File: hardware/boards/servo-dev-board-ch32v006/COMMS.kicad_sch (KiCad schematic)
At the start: 9 parts, among them J7 PIN-V, J8 PIN-V, J9 JST-PH-V, U4 74LVC2G241

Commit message: fix 74LVC2G241 footprint. Pin clearance was 0.15mm. PCBWay minimum is 0.2mm. Corrent Pin width is 0.3mm with pitch of 0.5mm, leaving 0.2mm clearance. Standard KiCad Library's pin width was 0.35mm, leaving only 0.15mm of clearance, which PCBWay rejected for their standard process.
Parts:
- U4: footprint Package_SO:VSSOP-8_2.3x2mm_P0.5mm -> shared:VSSOP-8_L2.3-W2.0-P0.50-LS3.1-BR
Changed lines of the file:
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@@
 			)
 		)
-		(property "Footprint" "Package_SO:VSSOP-8_2.3x2mm_P0.5mm"
+		(property "Footprint" "shared:VSSOP-8_L2.3-W2.0-P0.50-LS3.1-BR"
 			(at 80.01 87.63 0)
 			(effects
@@
 			)
 		)
-		(property "Footprint" "Package_SO:VSSOP-8_2.3x2mm_P0.5mm"
+		(property "Footprint" "shared:VSSOP-8_L2.3-W2.0-P0.50-LS3.1-BR"
 			(at 39.37 86.36 0)
 			(effects
@@
 			)
 		)
-		(property "Footprint" "Package_SO:VSSOP-8_2.3x2mm_P0.5mm"
+		(property "Footprint" "shared:VSSOP-8_L2.3-W2.0-P0.50-LS3.1-BR"
 			(at 102.87 87.63 0)
 			(effects

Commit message: updated LCSC part numbers for all symbols
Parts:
- C15: LCSC (none) -> C28233
- J7, J8: LCSC (none) -> C49257
- J9: LCSC (none) -> C131339
- R14, R15, R16: LCSC (none) -> C17414
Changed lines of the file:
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@@
+			)
+		)
+		(property "LCSC" "C28233"
+			(at 27.94 85.0899 0)
+			(effects
+				(font
+					(size 1.27 1.27)
+				)
+				(hide yes)
 			)
 		)
@@
 			)
 		)
+		(property "LCSC" "C17414"
+			(at 162.56 87.6299 0)
+			(effects
+				(font
+					(size 1.27 1.27)
+				)
+				(hide yes)
+			)
+		)
 		(pin "2"
 		)
@@
 			)
 		)
+		(property "LCSC" "C17414"
+			(at 149.86 87.6299 0)
+			(effects
+				(font
+					(size 1.27 1.27)
+				)
+				(hide yes)
+			)
+		)
 		(pin "2"
 		)
@@
 		(property "Description" "Generic connector, single row, 01x03, script generated (kicad-library-utils/schlib/autogen/connector/)"
 			(at 38.1 49.53 0)
+			(effects
+				(font
+					(size 1.27 1.27)
+				)
+				(hide yes)
+			)
+		)
+		(property "LCSC" "C49257"
+			(at 38.1 43.18 0)
 			(effects
 				(font
@@
 			)
 		)
+		(property "LCSC" "C49257"
+			(at 59.69 43.18 0)
+			(effects
+				(font
+					(size 1.27 1.27)
+				)
+				(hide yes)
+			)
+		)
 		(pin "2"
 		)
@@
 			)
 		)
+		(property "LCSC" "C17414"
+			(at 137.16 87.6299 0)
+			(effects
+				(font
+					(size 1.27 1.27)
+				)
+				(hide yes)
+			)
+		)
 		(pin "2"
 		)
@@
 			(effects
 				(font
+					(size 1.27 1.27)
+				)
+				(hide yes)
+			)
+		)
+		(property "LCSC" "C131339"
+			(at 104.14 43.18 0)
+			(effects
+				(font

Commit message: remove 'LCSC Part' Property from project
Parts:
- J9: LCSC Part C131339 -> (none)
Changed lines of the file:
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@@
-			)
-		)
-		(property "LCSC Part" "C131339"
-			(at 104.14 64.77 0)
-			(effects
-				(font
-					(size 1.27 1.27)
-				)
-				(hide yes)
 			)
 		)

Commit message: added MFPN properties
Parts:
- C15: MFPN (none) -> CL21B104KCFNNNE
- D4: MFPN (none) -> PESD5V0L1BA
- J7, J8: MFPN (none) -> 2.54-1*3P
- J9: MFPN (none) -> B3B-PH-K-S(LF)(SN)
- R14, R15, R16: MFPN (none) -> 0805W8F1002T5E
- U4: MFPN (none) -> SN74LVC2G241DCUR
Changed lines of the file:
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@@
+			)
+		)
+		(property "MFPN" "SN74LVC2G241DCUR"
+			(at 80.01 87.63 0)
+			(effects
+				(font
+					(size 1.27 1.27)
+				)
+				(hide yes)
 			)
 		)
@@
 			)
 		)
+		(property "MFPN" "CL21B104KCFNNNE"
+			(at 27.94 85.0899 0)
+			(effects
+				(font
+					(size 1.27 1.27)
+				)
+				(hide yes)
+			)
+		)
 		(pin "2"
 		)
@@
 			)
 		)
+		(property "MFPN" "PESD5V0L1BA"
+			(at 146.05 49.53 90)
+			(effects
+				(font
+					(size 1.27 1.27)
+				)
+				(hide yes)
+			)
+		)
 		(property "JLC Type" "Extended"
 			(at 146.05 49.53 90)
@@
 		)
 		(property "LCSC" "C17414"
+			(at 162.56 87.6299 0)
+			(effects
+				(font
+					(size 1.27 1.27)
+				)
+				(hide yes)
+			)
+		)
+		(property "MFPN" "0805W8F1002T5E"
 			(at 162.56 87.6299 0)
 			(effects
@@
 			)
 		)
+		(property "MFPN" "0805W8F1002T5E"
+			(at 149.86 87.6299 0)
+			(effects
+				(font
+					(size 1.27 1.27)
+				)
+				(hide yes)
+			)
+		)
 		(pin "2"
 		)
@@
 			)
 		)
+		(property "MFPN" "2.54-1*3P"
+			(at 38.1 43.18 0)
+			(effects
+				(font
+					(size 1.27 1.27)
+				)
+				(hide yes)
+			)
+		)
 		(pin "2"
 		)
@@
 			)
 		)
+		(property "MFPN" "SN74LVC2G241DCUR"
+			(at 39.37 86.36 0)
+			(effects
+				(font
+					(size 1.27 1.27)
+				)
+				(hide yes)
+			)
+		)
 		(property "JLC Type" "Extended"
 			(at 39.37 86.36 0)
@@
 			)
 		)
+		(property "MFPN" "2.54-1*3P"
+			(at 59.69 43.18 0)
+			(effects
+				(font
+					(size 1.27 1.27)
+				)
+				(hide yes)
+			)
+		)
 		(pin "2"
 		)
@@
 			)
 		)
+		(property "MFPN" "0805W8F1002T5E"
+			(at 137.16 87.6299 0)
+			(effects
+				(font
+					(size 1.27 1.27)
+				)
+				(hide yes)
+			)
+		)
 		(pin "2"
 		)
@@
 			)
 		)
+		(property "MFPN" "B3B-PH-K-S(LF)(SN)"
+			(at 104.14 43.18 0)
+			(effects
+				(font
+					(size 1.27 1.27)
+				)
+				(hide yes)
+			)
+		)
 		(pin "3"
 		)
@@
 			(at 102.87 87.63 0)
 			(effects
+				(font
+					(size 1.27 1.27)
+				)
+				(hide yes)
+			)
+		)
+		(property "MFPN" "SN74LVC2G241DCUR"
+			(at 102.87 87.63 0)
+			(effects

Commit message: update board
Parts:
- added JP2: TLL | UART, Connector_PinHeader_2.54mm:PinHeader_1x03_P2.54mm_Vertical, symbol Jumper:Jumper_3_Open
- renumbered C15 to C12, D4 to D5, J9 to J10, J7 to J8, J8 to J9, R14 to R15, R15 to R16, R16 to R17
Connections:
- net RX: now also JP2.3 (B); no longer U4.6
- new net JP_RX: JP2.2 (C), U4.6
- no-connect marks 0 -> 1
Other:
- note added: "UART / TTL SELECTION"

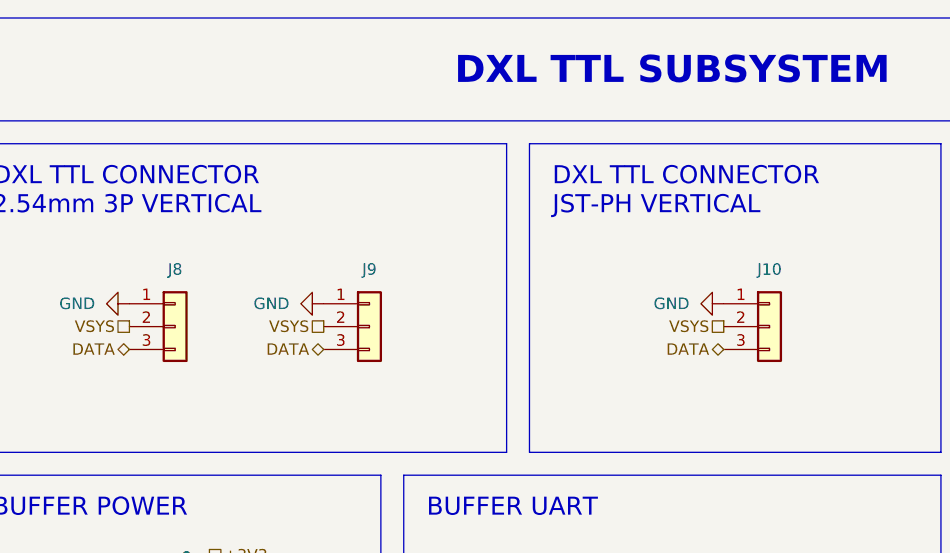
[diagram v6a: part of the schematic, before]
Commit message: updated schematics. ERC on schematics is now passing
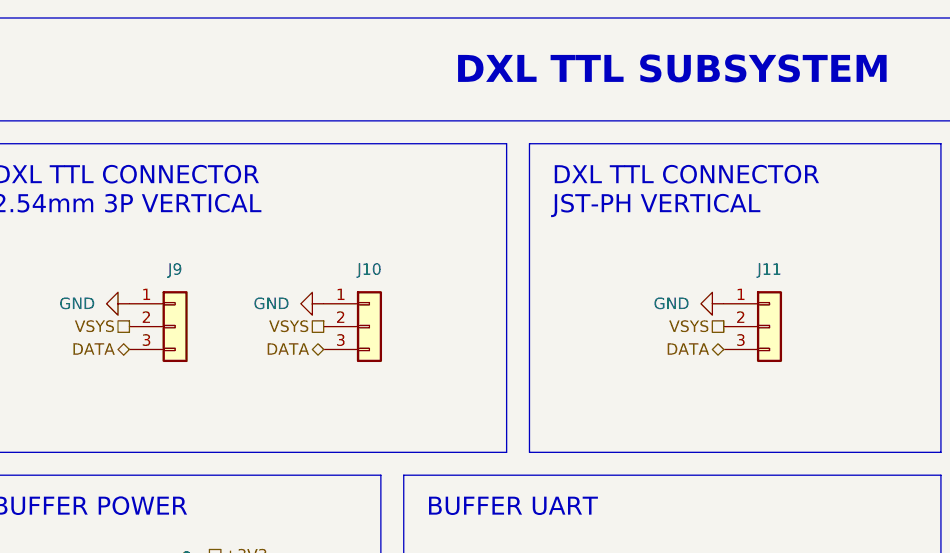
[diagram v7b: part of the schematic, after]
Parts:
- renumbered J9 to J10, J10 to J11, J8 to J9
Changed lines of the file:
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@@
 		(in_pos_files yes)
 		(dnp no)
-		(property "Reference" "#PWR044"
+		(property "Reference" "#PWR050"
 			(at 48.26 46.99 0)
 			(hide yes)
@@
 			(project "servo-dev-board-ch32v006"
 				(path "/6062e7d2-0c72-467e-b49c-6387ba053e09/d650f1be-e012-4c20-9ca8-eaa5ec4968ee"
-					(reference "#PWR044")
+					(reference "#PWR050")
 					(unit 1)
 				)
@@
 		(in_pos_files yes)
 		(dnp no)
-		(property "Reference" "#PWR042"
+		(property "Reference" "#PWR048"
 			(at 26.67 46.99 0)
 			(hide yes)
@@
 			(project "servo-dev-board-ch32v006"
 				(path "/6062e7d2-0c72-467e-b49c-6387ba053e09/d650f1be-e012-4c20-9ca8-eaa5ec4968ee"
-					(reference "#PWR042")
+					(reference "#PWR048")
 					(unit 1)
 				)
@@
 		(dnp no)
 		(fields_autoplaced yes)
-		(property "Reference" "#PWR046"
+		(property "Reference" "#PWR052"
 			(at 146.05 59.69 0)
 			(hide yes)
@@
 			(project "servo-dev-board-ch32v006"
 				(path "/6062e7d2-0c72-467e-b49c-6387ba053e09/d650f1be-e012-4c20-9ca8-eaa5ec4968ee"
-					(reference "#PWR046")
+					(reference "#PWR052")
 					(unit 1)
 				)
@@
 		(in_pos_files yes)
 		(dnp no)
-		(property "Reference" "#PWR045"
+		(property "Reference" "#PWR051"
 			(at 92.71 46.99 0)
 			(hide yes)
@@
 			(project "servo-dev-board-ch32v006"
 				(path "/6062e7d2-0c72-467e-b49c-6387ba053e09/d650f1be-e012-4c20-9ca8-eaa5ec4968ee"
-					(reference "#PWR045")
+					(reference "#PWR051")
 					(unit 1)
 				)
@@
 		(in_pos_files yes)
 		(dnp no)
-		(property "Reference" "J8"
+		(property "Reference" "J9"
 			(at 38.1 43.18 0)
 			(show_name no)
@@
 			(project "servo-dev-board-ch32v006"
 				(path "/6062e7d2-0c72-467e-b49c-6387ba053e09/d650f1be-e012-4c20-9ca8-eaa5ec4968ee"
-					(reference "J8")
+					(reference "J9")
 					(unit 1)
 				)
@@
 		(in_pos_files yes)
 		(dnp no)
-		(property "Reference" "J9"
+		(property "Reference" "J10"
 			(at 59.69 43.18 0)
 			(show_name no)
@@
 			(project "servo-dev-board-ch32v006"
 				(path "/6062e7d2-0c72-467e-b49c-6387ba053e09/d650f1be-e012-4c20-9ca8-eaa5ec4968ee"
-					(reference "J9")
+					(reference "J10")
 					(unit 1)
 				)
@@
 		(in_pos_files yes)
 		(dnp no)
-		(property "Reference" "J10"
+		(property "Reference" "J11"
 			(at 104.14 43.18 0)
 			(show_name no)
@@
 			(project "servo-dev-board-ch32v006"
 				(path "/6062e7d2-0c72-467e-b49c-6387ba053e09/d650f1be-e012-4c20-9ca8-eaa5ec4968ee"
-					(reference "J10")
+					(reference "J11")
 					(unit 1)
 				)
@@
 		(dnp no)
 		(fields_autoplaced yes)
-		(property "Reference" "#PWR047"
+		(property "Reference" "#PWR053"
 			(at 147.32 99.06 0)
 			(hide yes)
@@
 			(project "servo-dev-board-ch32v006"
 				(path "/6062e7d2-0c72-467e-b49c-6387ba053e09/d650f1be-e012-4c20-9ca8-eaa5ec4968ee"
-					(reference "#PWR047")
+					(reference "#PWR053")
 					(unit 1)
 				)
@@
 		(dnp no)
 		(fields_autoplaced yes)
-		(property "Reference" "#PWR043"
+		(property "Reference" "#PWR049"
 			(at 39.37 105.41 0)
 			(hide yes)
@@
 			(project "servo-dev-board-ch32v006"
 				(path "/6062e7d2-0c72-467e-b49c-6387ba053e09/d650f1be-e012-4c20-9ca8-eaa5ec4968ee"
-					(reference "#PWR043")
+					(reference "#PWR049")
 					(unit 1)
 				)

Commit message: completed routing.
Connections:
- net JP_RX: now also JP2.3 (B); no longer JP2.2 (C)
- net RX: now also JP2.2 (C); no longer JP2.3 (B)
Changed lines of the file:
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@@
 	(wire
 		(pts
-			(xy 39.37 123.19) (xy 39.37 130.81)
-		)
-		(stroke
-			(width 0)
-			(type default)
-		)
-	)
-	(wire
-		(pts
-			(xy 31.75 134.62) (xy 34.29 134.62)
+			(xy 39.37 128.27) (xy 39.37 130.81)
+		)
+		(stroke
+			(width 0)
+			(type default)
+		)
+	)
+	(wire
+		(pts
+			(xy 26.67 134.62) (xy 34.29 134.62)
 		)
 		(stroke
@@
 			(width 0)
 			(type default)
-		)
-	)
-	(label "JP_RX"
-		(at 39.37 123.19 270)
-		(effects
-			(font
-				(size 1.27 1.27)
-			)
-			(justify right bottom)
 		)
 	)
 	(label "JP_RX"
 		(at 64.77 87.63 0)
+		(effects
+			(font
+				(size 1.27 1.27)
+			)
+			(justify left bottom)
+		)
+	)
+	(label "JP_RX"
+		(at 26.67 134.62 0)
 		(effects
 			(font
@@
 		)
 	)
-	(hierarchical_label "RX"
-		(shape output)
-		(at 31.75 134.62 180)
-		(effects
-			(font
-				(size 1.27 1.27)
-			)
-			(justify right)
-		)
-	)
 	(hierarchical_label "VSYS"
 		(shape passive)
@@
 		(effects
 			(font
+				(size 1.27 1.27)
+			)
+			(justify left)
+		)
+	)
+	(hierarchical_label "RX"
+		(shape output)
+		(at 39.37 128.27 90)
+		(effects
+			(font
